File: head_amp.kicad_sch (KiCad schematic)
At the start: 23 parts, among them J1 Conn_01x15, J2 Conn_01x15, J3 Left_Speaker, J4 Left_Mic, J5 Right_Speaker, J6 Right_Mic, J7 Conn_01x03, J8 Conn_01x03, M1 Fan, Q1 AO3401A, Q2 AO3400A, Q3 AO3400A, U1 LSM6DS3, U2 PJ-320A

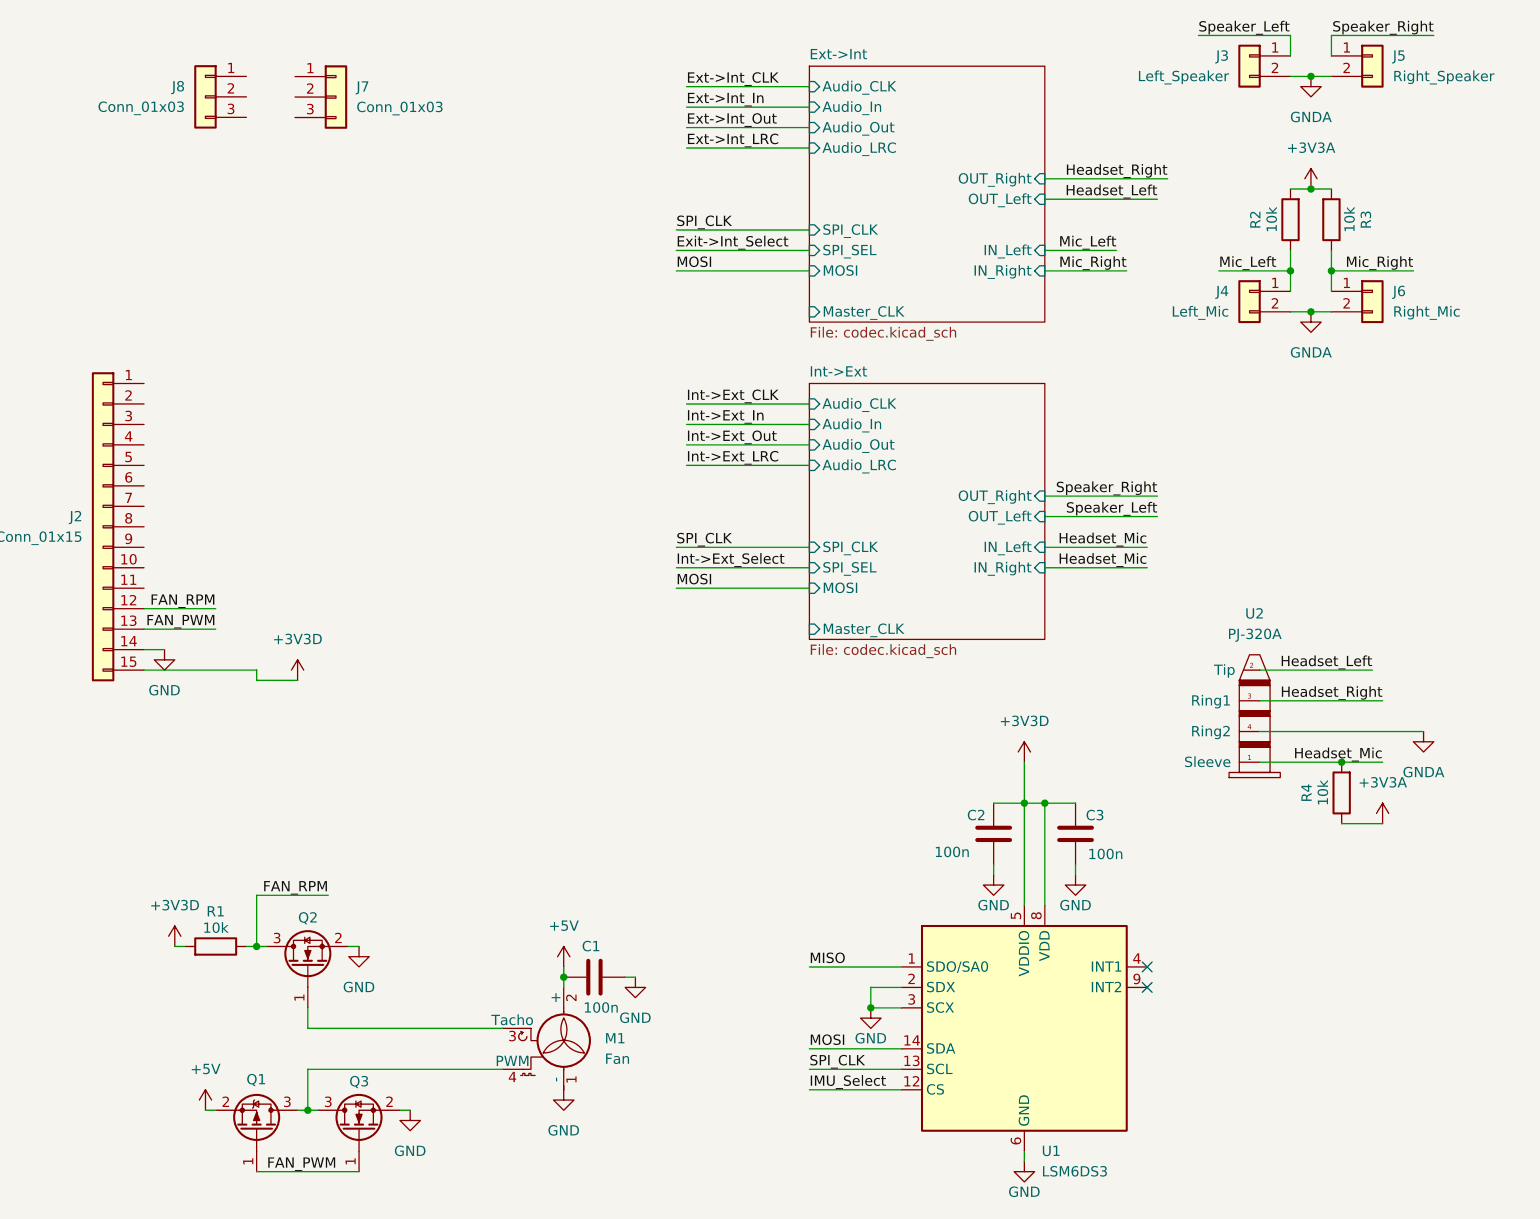
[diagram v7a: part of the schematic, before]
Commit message: More capacitor layed
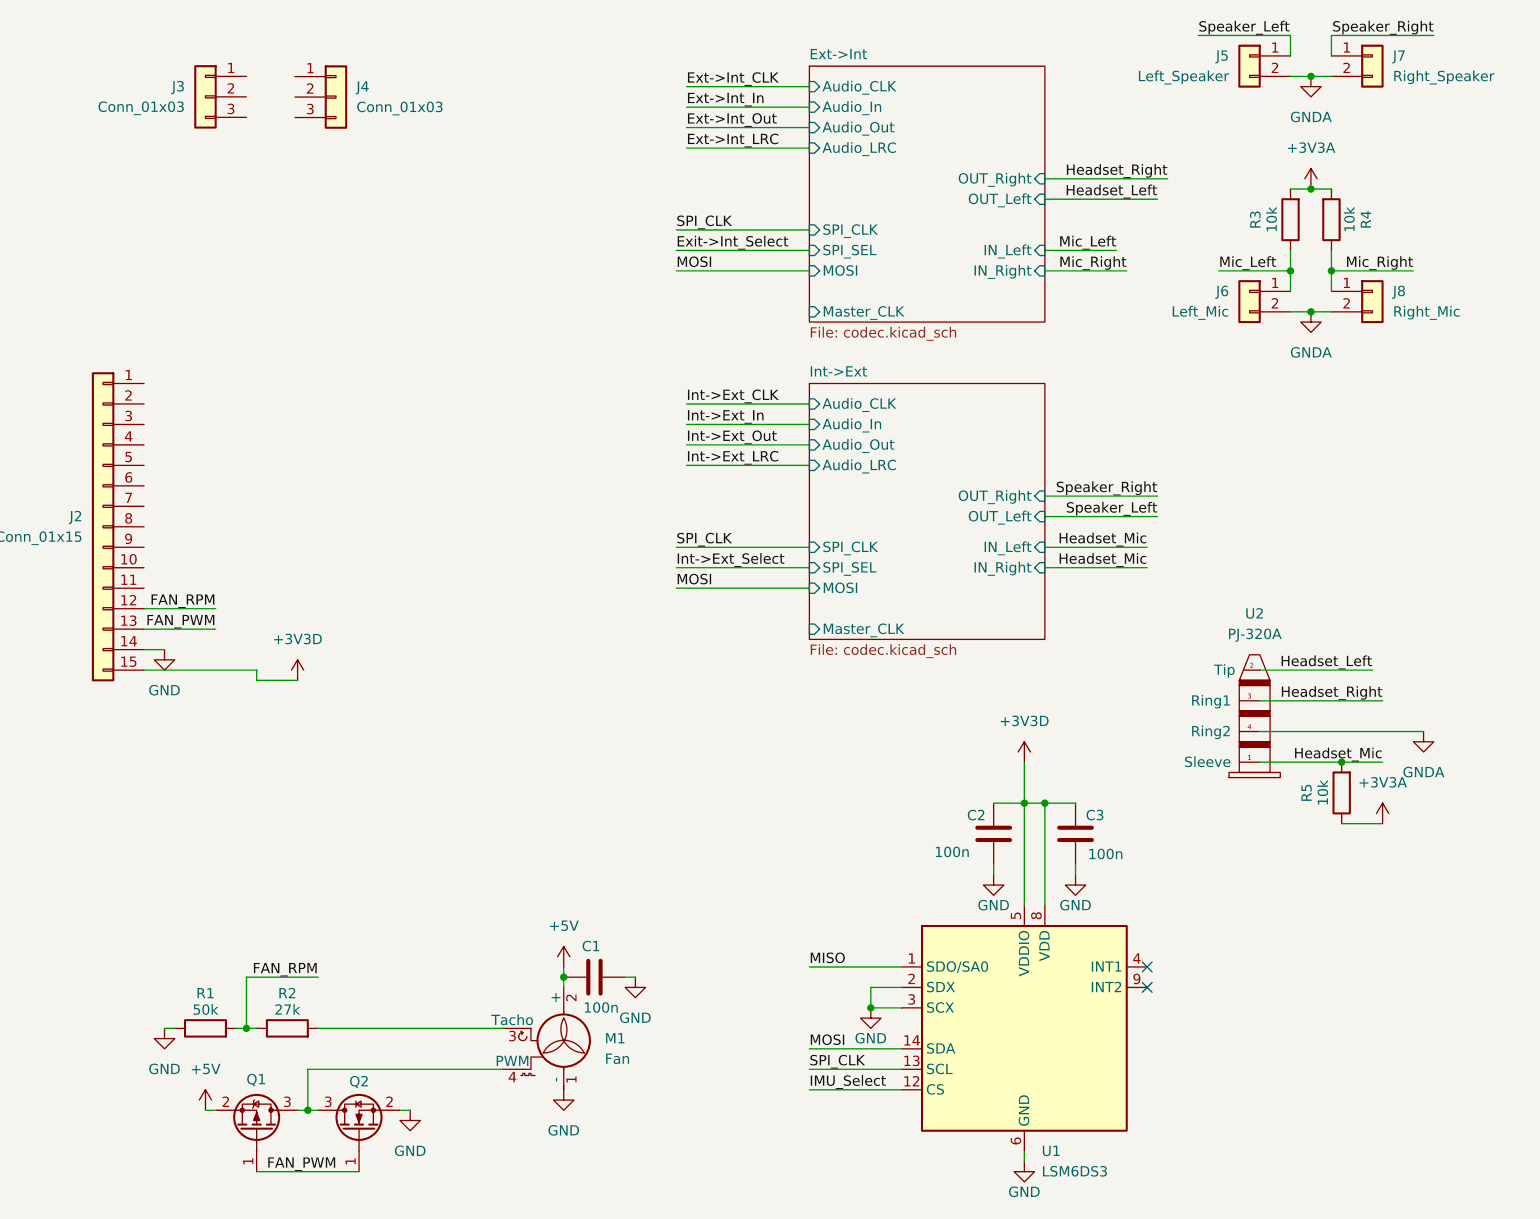
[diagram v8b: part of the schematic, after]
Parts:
- removed Q2: AO3400A, Package_TO_SOT_SMD:SOT-23, symbol Transistor_FET:AO3400A
- added R2: 27k, Resistor_SMD:R_0603_1608Metric, symbol Device:R
- R1: value 10k -> 50k
- renumbered J8 to J3, J7 to J4, J3 to J5, J4 to J6, J5 to J7, J6 to J8, Q3 to Q2, R2 to R3, R3 to R4, R4 to R5
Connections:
- net +3V3D: no longer R1.2
- net FAN_RPM: now also R1.2, R2.1; no longer R1.1
- net GND: now also R1.1
- net at M1.3 (Tacho): now also R2.2
